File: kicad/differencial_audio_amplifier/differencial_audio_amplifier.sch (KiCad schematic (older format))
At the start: 35 parts, among them P1 CONN_01X03, P2 CONN_01X03, P3 CONN_01X03, U3 LM358

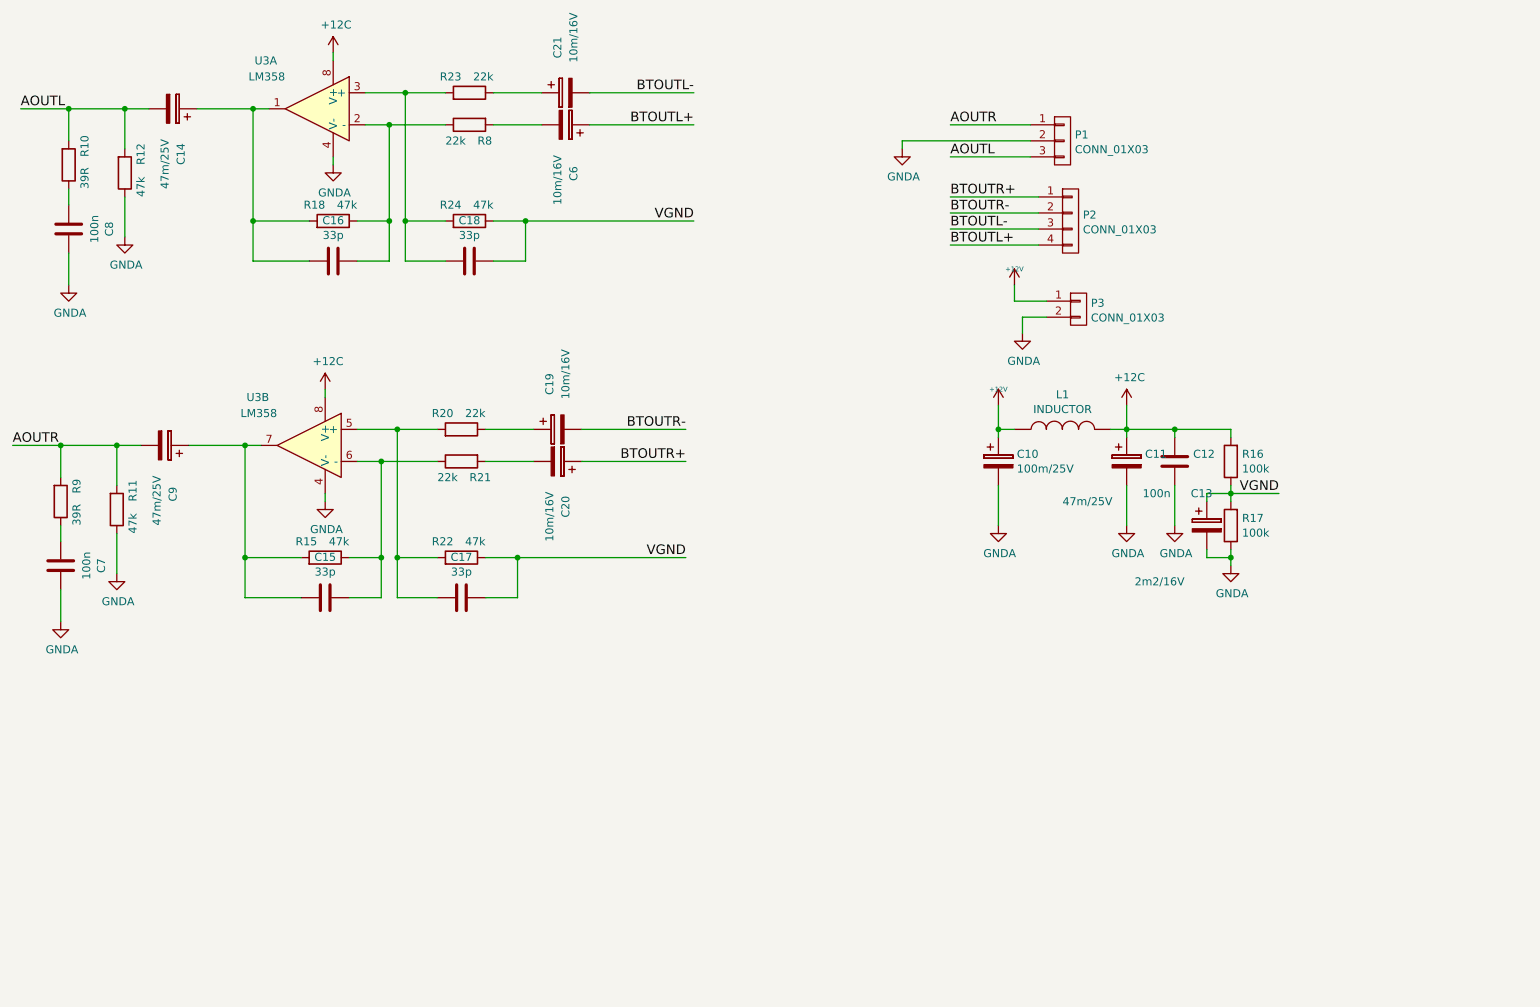
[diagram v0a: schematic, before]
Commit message: change LM358 to ne5532, same pics from net with actual module, sold by elecfreeks
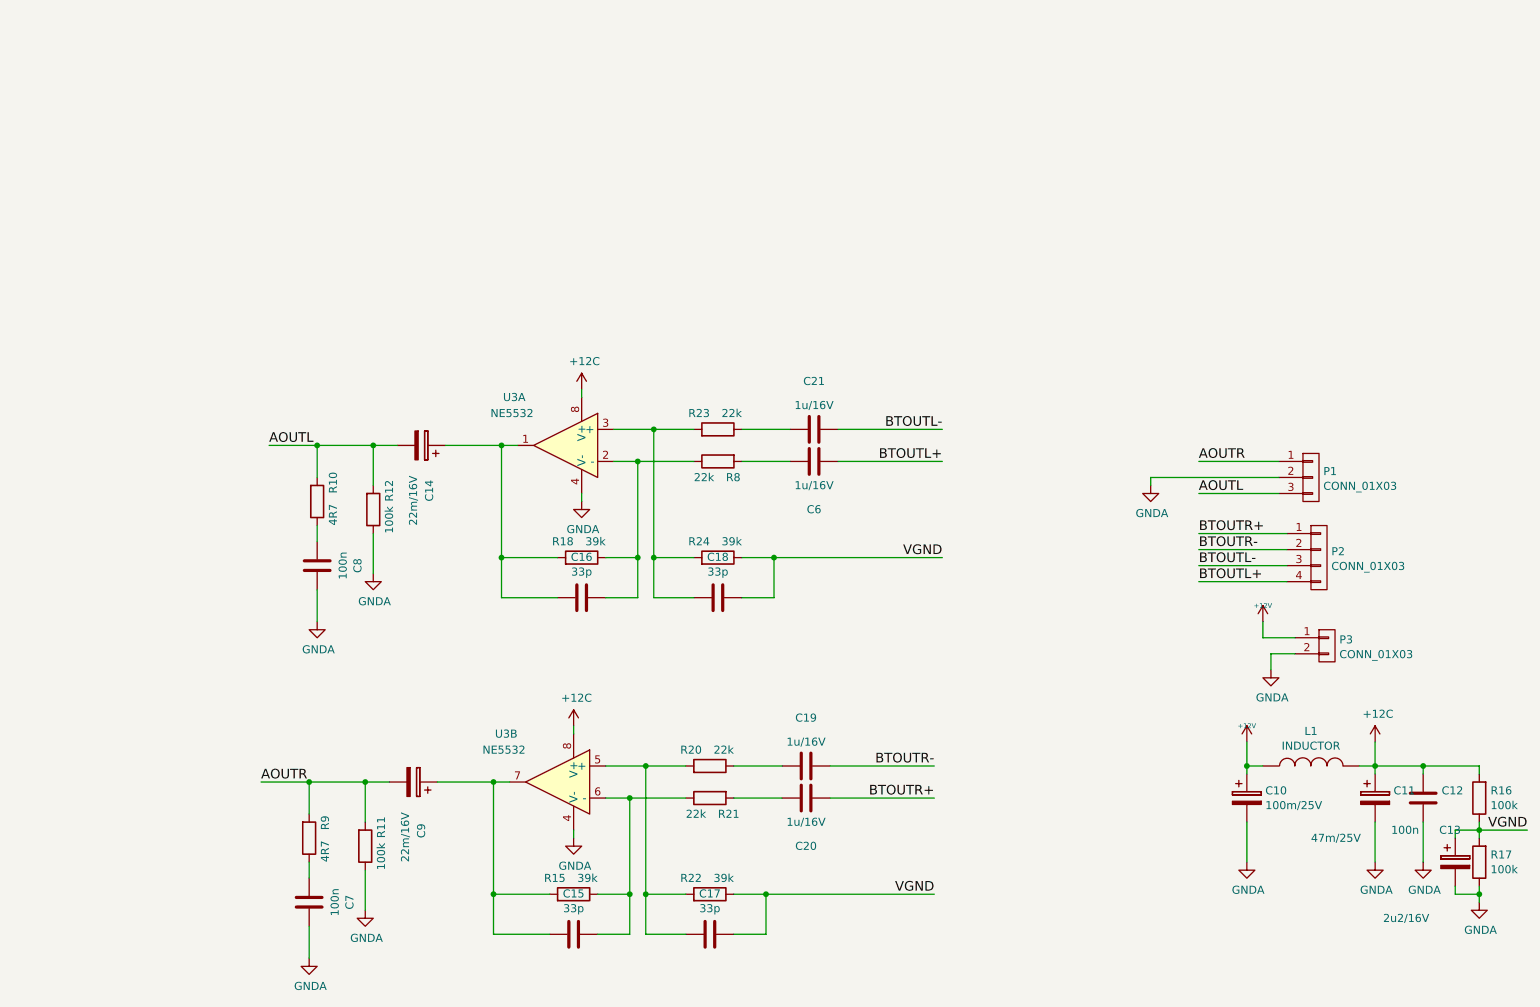
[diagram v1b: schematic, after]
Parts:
- removed C19, C20, C21, C6: 10m/16V, Capacitors_SMD:c_elec_5x5.8, symbol CP
- added C19, C20, C21, C6: 1u/16V, Capacitors_SMD:C_0805_HandSoldering, symbol C
- C13: value 2m2/16V -> 2u2/16V
- C14, C9: value 47m/25V -> 22m/16V; footprint Capacitors_SMD:c_elec_6.3x5.7 -> Capacitors_SMD:c_elec_5x5.3
- R10, R9: value 39R -> 4R7
- R11, R12: value 47k -> 100k
- R15, R18, R22, R24: value 47k -> 39k
- U3: value LM358 -> NE5532
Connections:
- net BTOUTL+: now also C6.1
- net BTOUTL-: now also C21.2
- net BTOUTR+: now also C20.1
- net BTOUTR-: now also C19.2
- net at R8.2: now also C6.2
- net at R23.1: now also C21.1
- net at R21.2: now also C20.2
- net at R20.1: now also C19.1
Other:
- moved on the sheet: C10, C11, C12, C13, C14, C15, C16, C17, C18, C7, C8, C9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
